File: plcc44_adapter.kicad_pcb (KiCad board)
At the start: 2 copper layers, 25.4 x 52.1 mm, 2 parts, among them U1 ATmega8515-16JU, U2 PIC16F74-IP

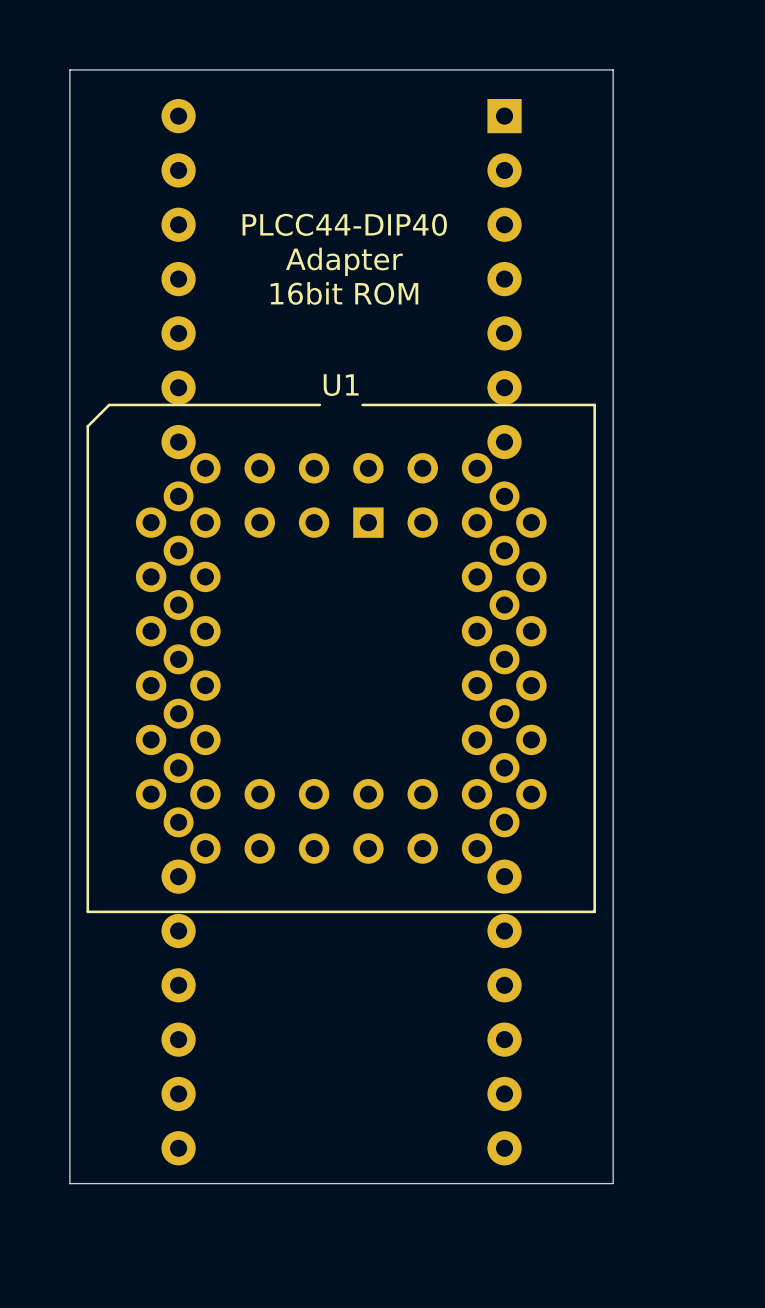
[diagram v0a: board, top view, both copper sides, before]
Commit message: Updated Symbols Updates Footprints for easier soldering
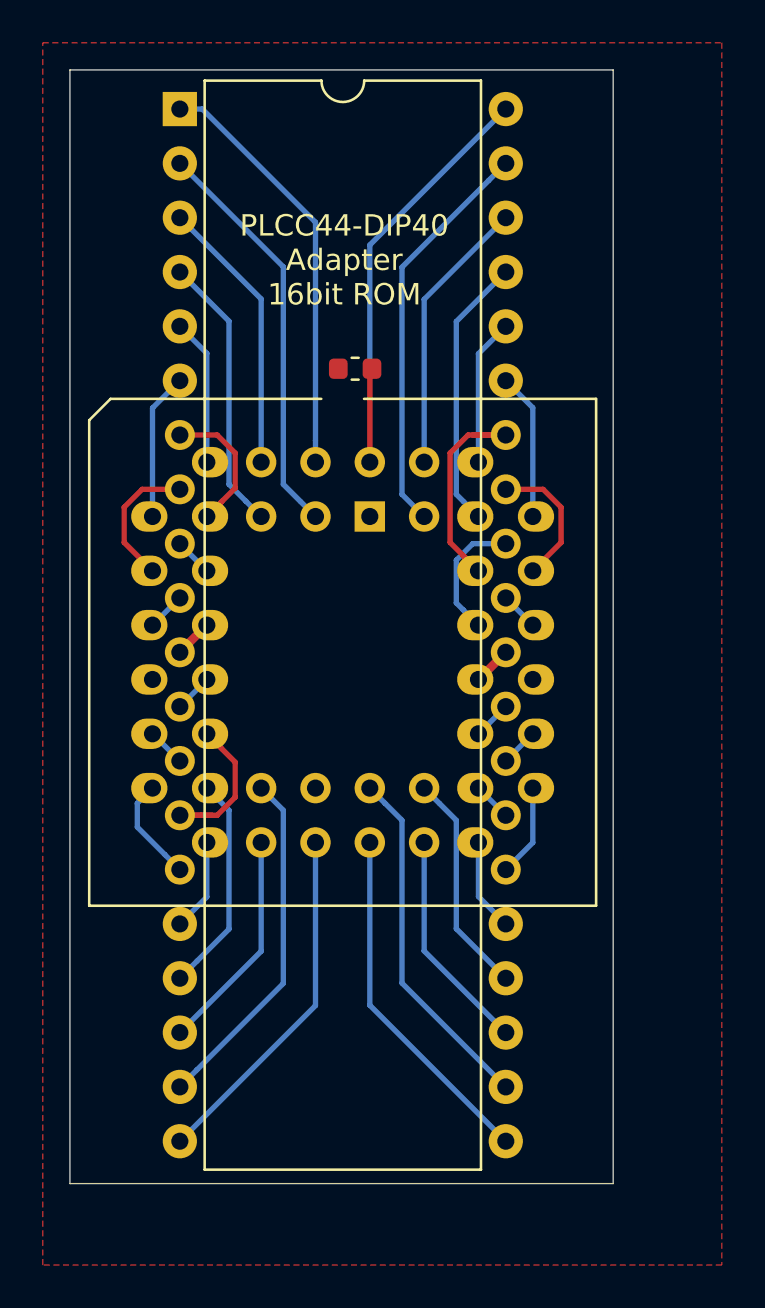
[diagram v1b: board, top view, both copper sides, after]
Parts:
- added C1: 100nF, Capacitor_SMD:C_0603_1608Metric, F.Cu at (173.4, 66.0)
- U1: value ATmega8515-16JU -> 16bit_rom; footprint Package_LCC:PLCC-44_THT-Socket -> dip40_mod:PLCC-44_THT-Socket_mod
- U2: value PIC16F74-IP -> 16bit_rom_dip40; footprint Package_DIP:DIP-40_W15.24mm -> dip40_mod:DIP-40_W15.24mm_mod; moved to F.Cu
- moved U2 15.2 mm to (165.2, 53.9), turned to 0 degrees
- moved U1 0.29 mm to (174.0, 72.9)
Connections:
- U1 pad 1: Net-(U1-Pad1) -> (no net)
- U1 pad 12: Net-(U1-Pad12) -> GND
- U1 pad 13: Net-(U1-Pad13) -> (no net)
- U1 pad 23: Net-(U1-Pad23) -> (no net)
- U1 pad 33: Net-(U1-Pad33) -> (no net)
- U1 pad 34: Net-(U1-Pad34) -> GND
- U1 pad 44: Net-(U1-Pad44) -> Net-(C1-Pad1)
- U2 pad 1: Net-(U2-Pad1) -> Net-(U1-Pad2)
- U2 pad 10: Net-(U2-Pad10) -> Net-(U1-Pad11)
- U2 pad 11: Net-(U2-Pad11) -> GND
- U2 pad 12: Net-(U2-Pad12) -> Net-(U1-Pad14)
- U2 pad 13: Net-(U2-Pad13) -> Net-(U1-Pad15)
- U2 pad 14: Net-(U2-Pad14) -> Net-(U1-Pad16)
- U2 pad 15: Net-(U2-Pad15) -> Net-(U1-Pad17)
- U2 pad 16: Net-(U2-Pad16) -> Net-(U1-Pad18)
- U2 pad 17: Net-(U2-Pad17) -> Net-(U1-Pad19)
- U2 pad 18: Net-(U2-Pad18) -> Net-(U1-Pad20)
- U2 pad 19: Net-(U2-Pad19) -> Net-(U1-Pad21)
- U2 pad 2: Net-(U2-Pad2) -> Net-(U1-Pad3)
- U2 pad 20: Net-(U2-Pad20) -> Net-(U1-Pad22)
- U2 pad 21: Net-(U2-Pad21) -> Net-(U1-Pad24)
- U2 pad 22: Net-(U2-Pad22) -> Net-(U1-Pad25)
- U2 pad 23: Net-(U2-Pad23) -> Net-(U1-Pad26)
- U2 pad 24: Net-(U2-Pad24) -> Net-(U1-Pad27)
- U2 pad 25: Net-(U2-Pad25) -> Net-(U1-Pad28)
- U2 pad 26: Net-(U2-Pad26) -> Net-(U1-Pad29)
- U2 pad 27: Net-(U2-Pad27) -> Net-(U1-Pad30)
- U2 pad 28: Net-(U2-Pad28) -> Net-(U1-Pad31)
- U2 pad 29: Net-(U2-Pad29) -> Net-(U1-Pad32)
- U2 pad 3: Net-(U2-Pad3) -> Net-(U1-Pad4)
- U2 pad 30: Net-(U2-Pad30) -> GND
- U2 pad 31: Net-(U2-Pad31) -> Net-(U1-Pad35)
- U2 pad 32: Net-(U2-Pad32) -> Net-(U1-Pad36)
- U2 pad 33: Net-(U2-Pad33) -> Net-(U1-Pad37)
- U2 pad 34: Net-(U2-Pad34) -> Net-(U1-Pad38)
- U2 pad 35: Net-(U2-Pad35) -> Net-(U1-Pad39)
- U2 pad 36: Net-(U2-Pad36) -> Net-(U1-Pad40)
- U2 pad 37: Net-(U2-Pad37) -> Net-(U1-Pad41)
- U2 pad 38: Net-(U2-Pad38) -> Net-(U1-Pad42)
- U2 pad 39: Net-(U2-Pad39) -> Net-(U1-Pad43)
- U2 pad 4: Net-(U2-Pad4) -> Net-(U1-Pad5)
- U2 pad 40: Net-(U2-Pad40) -> Net-(C1-Pad1)
- U2 pad 5: Net-(U2-Pad5) -> Net-(U1-Pad6)
- U2 pad 6: Net-(U2-Pad6) -> Net-(U1-Pad7)
- U2 pad 7: Net-(U2-Pad7) -> Net-(U1-Pad8)
- U2 pad 8: Net-(U2-Pad8) -> Net-(U1-Pad9)
- U2 pad 9: Net-(U2-Pad9) -> Net-(U1-Pad10)
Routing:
- net Net-(C1-Pad1): track 0.00 -> 23.7 mm
- net Net-(U1-Pad2): track 0.00 -> 19.8 mm
- net Net-(U1-Pad3): track 0.00 -> 19.1 mm
- net Net-(U1-Pad43): track 0.00 -> 18.9 mm
- net Net-(U1-Pad25): track 0.00 -> 16.6 mm
- net Net-(U1-Pad24): track 0.00 -> 16.6 mm
- net Net-(U1-Pad22): track 0.00 -> 16.6 mm
- net Net-(U1-Pad21): track 0.00 -> 16.4 mm
- net Net-(U1-Pad42): track 0.00 -> 13.0 mm
- net Net-(U1-Pad5): track 0.00 -> 13.0 mm
- net Net-(U1-Pad4): track 0.00 -> 13.0 mm
- net Net-(U1-Pad41): track 0.00 -> 12.8 mm
- net Net-(U1-Pad38): track 0.00 -> 11.6 mm
- net Net-(U1-Pad27): track 0.00 -> 10.5 mm
- net Net-(U1-Pad26): track 0.00 -> 10.5 mm
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- added copper zone on F.Cu, net GND
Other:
- net class GND added: clearance 0.2, trace_width 0.4, via_dia 0.8, via_drill 0.4

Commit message: Added Gerber Files Updated README Updated Layout
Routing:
- net Net-(C1-Pad1): track 23.7 -> 19.4 mm, vias 0 -> 1
- net Net-(U1-Pad17): track 4.93 -> 4.34 mm
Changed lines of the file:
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@@
     (thickness 1.6)
     (drawings 6)
-    (tracks 122)
+    (tracks 125)
     (zones 0)
     (modules 3)
@@
       (outputformat 1)
       (mirror false)
-      (drillshape 1)
+      (drillshape 0)
       (scaleselection 1)
-      (outputdirectory ""))
+      (outputdirectory "gerber"))
   )
   (net 0 "")
@@
   (gr_line (start 160.02 104.14) (end 185.42 104.14) (layer Edge.Cuts) (width 0.05))
   (gr_line (start 160.02 52.07) (end 160.02 104.14) (layer Edge.Cuts) (width 0.05))
+  (segment (start 170.2054 71.6534) (end 170.789601 72.237601) (width 0.25) (layer B.Cu) (net 1))
+  (segment (start 165.159001 56.439001) (end 170.2054 61.4854) (width 0.25) (layer B.Cu) (net 1))
   (segment (start 170.789601 72.237601) (end 171.5008 72.9488) (width 0.25) (layer B.Cu) (net 1))
-  (segment (start 169.997001 71.445001) (end 170.789601 72.237601) (width 0.25) (layer B.Cu) (net 1))
-  (segment (start 169.997001 61.277001) (end 169.997001 71.445001) (width 0.25) (layer B.Cu) (net 1))
-  (segment (start 165.159001 56.439001) (end 169.997001 61.277001) (width 0.25) (layer B.Cu) (net 1))
-  (segment (start 167.457001 71.445001) (end 168.249601 72.237601) (width 0.25) (layer B.Cu) (net 2))
-  (segment (start 167.457001 63.817001) (end 167.457001 71.445001) (width 0.25) (layer B.Cu) (net 2))
+  (segment (start 170.2054 61.4854) (end 170.2054 71.6534) (width 0.25) (layer B.Cu) (net 1))
+  (segment (start 167.7924 71.7804) (end 168.249601 72.237601) (width 0.25) (layer B.Cu) (net 2))
+  (segment (start 165.159001 61.519001) (end 167.7924 64.1524) (width 0.25) (layer B.Cu) (net 2))
   (segment (start 168.249601 72.237601) (end 168.9608 72.9488) (width 0.25) (layer B.Cu) (net 2))
-  (segment (start 165.159001 61.519001) (end 167.457001 63.817001) (width 0.25) (layer B.Cu) (net 2))
+  (segment (start 167.7924 64.1524) (end 167.7924 71.7804) (width 0.25) (layer B.Cu) (net 2))
   (segment (start 179.599002 57.239) (end 180.399001 56.439001) (width 0.25) (layer B.Cu) (net 3))
-  (segment (start 175.544599 61.293403) (end 179.599002 57.239) (width 0.25) (layer B.Cu) (net 3))
-  (segment (start 175.544599 71.912599) (end 175.544599 61.293403) (width 0.25) (layer B.Cu) (net 3))
-  (segment (start 176.5808 72.9488) (end 175.544599 71.912599) (width 0.25) (layer B.Cu) (net 3))
+  (segment (start 175.3108 61.527202) (end 179.599002 57.239) (width 0.25) (layer B.Cu) (net 3))
+  (segment (start 176.5808 72.9488) (end 175.3108 71.6788) (width 0.25) (layer B.Cu) (net 3))
+  (segment (start 175.3108 71.6788) (end 175.3108 61.527202) (width 0.25) (layer B.Cu) (net 3))
   (segment (start 178.409601 72.237601) (end 179.1208 72.9488) (width 0.25) (layer B.Cu) (net 4))
-  (segment (start 178.084599 63.833403) (end 178.084599 71.912599) (width 0.25) (layer B.Cu) (net 4))
-  (segment (start 178.084599 71.912599) (end 178.409601 72.237601) (width 0.25) (layer B.Cu) (net 4))
-  (segment (start 180.399001 61.519001) (end 178.084599 63.833403) (width 0.25) (layer B.Cu) (net 4))
+  (segment (start 180.399001 61.519001) (end 177.673 64.245002) (width 0.25) (layer B.Cu) (net 4))
+  (segment (start 177.673 71.501) (end 178.409601 72.237601) (width 0.25) (layer B.Cu) (net 4))
+  (segment (start 177.673 64.245002) (end 177.673 71.501) (width 0.25) (layer B.Cu) (net 4))
   (segment (start 171.5008 59.1908) (end 171.5008 69.403012) (width 0.25) (layer B.Cu) (net 5))
   (segment (start 166.209001 53.899001) (end 171.5008 59.1908) (width 0.25) (layer B.Cu) (net 5))
@@
   (segment (start 166.4208 70.4088) (end 166.4208 65.3208) (width 0.25) (layer B.Cu) (net 7))
   (segment (start 174.0408 60.257202) (end 180.399001 53.899001) (width 0.25) (layer B.Cu) (net 39))
-  (segment (start 174.0408 70.4088) (end 174.0408 60.257202) (width 0.25) (layer B.Cu) (net 39))
   (segment (start 176.5808 62.797202) (end 176.5808 70.4088) (width 0.25) (layer B.Cu) (net 8))
   (segment (start 180.399001 58.979001) (end 176.5808 62.797202) (width 0.25) (layer B.Cu) (net 8))
@@
   (segment (start 163.8888 83.1088) (end 165.159001 84.379001) (width 0.25) (layer B.Cu) (net 16))
   (segment (start 163.8808 83.1088) (end 163.8888 83.1088) (width 0.25) (layer B.Cu) (net 16))
+  (segment (start 163.8808 85.6488) (end 163.8808 88.1808) (width 0.25) (layer B.Cu) (net 17))
   (segment (start 164.459002 88.759002) (end 165.159001 89.459001) (width 0.25) (layer B.Cu) (net 17))
-  (segment (start 163.169601 86.359999) (end 163.169601 87.469601) (width 0.25) (layer B.Cu) (net 17))
-  (segment (start 163.169601 87.469601) (end 164.459002 88.759002) (width 0.25) (layer B.Cu) (net 17))
-  (segment (start 163.8808 85.6488) (end 163.169601 86.359999) (width 0.25) (layer B.Cu) (net 17))
+  (segment (start 163.8808 88.1808) (end 164.459002 88.759002) (width 0.25) (layer B.Cu) (net 17))
+  (segment (start 167.8178 91.880202) (end 165.959 93.739002) (width 0.25) (layer B.Cu) (net 18))
   (segment (start 165.959 93.739002) (end 165.159001 94.539001) (width 0.25) (layer B.Cu) (net 18))
-  (segment (start 167.457001 92.241001) (end 165.959 93.739002) (width 0.25) (layer B.Cu) (net 18))
-  (segment (start 167.457001 86.685001) (end 167.457001 92.241001) (width 0.25) (layer B.Cu) (net 18))
-  (segment (start 166.4208 85.6488) (end 167.457001 86.685001) (width 0.25) (layer B.Cu) (net 18))
+  (segment (start 166.4208 85.6488) (end 167.8178 87.0458) (width 0.25) (layer B.Cu) (net 18))
+  (segment (start 167.8178 87.0458) (end 167.8178 91.880202) (width 0.25) (layer B.Cu) (net 18))
   (segment (start 165.959 98.819002) (end 165.159001 99.619001) (width 0.25) (layer B.Cu) (net 19))
-  (segment (start 169.997001 94.781001) (end 165.959 98.819002) (width 0.25) (layer B.Cu) (net 19))
-  (segment (start 169.997001 86.685001) (end 169.997001 94.781001) (width 0.25) (layer B.Cu) (net 19))
-  (segment (start 168.9608 85.6488) (end 169.997001 86.685001) (width 0.25) (layer B.Cu) (net 19))
-  (segment (start 175.544599 87.152599) (end 174.751999 86.359999) (width 0.25) (layer B.Cu) (net 20))
+  (segment (start 170.2054 94.572602) (end 165.959 98.819002) (width 0.25) (layer B.Cu) (net 19))
+  (segment (start 168.9608 85.6488) (end 170.2054 86.8934) (width 0.25) (layer B.Cu) (net 19))
+  (segment (start 170.2054 86.8934) (end 170.2054 94.572602) (width 0.25) (layer B.Cu) (net 19))
   (segment (start 174.751999 86.359999) (end 174.0408 85.6488) (width 0.25) (layer B.Cu) (net 20))
-  (segment (start 175.544599 94.764599) (end 175.544599 87.152599) (width 0.25) (layer B.Cu) (net 20))
-  (segment (start 180.399001 99.619001) (end 175.544599 94.764599) (width 0.25) (layer B.Cu) (net 20))
+  (segment (start 180.399001 99.619001) (end 175.3362 94.5562) (width 0.25) (layer B.Cu) (net 20))
+  (segment (start 175.3362 86.9442) (end 174.751999 86.359999) (width 0.25) (layer B.Cu) (net 20))
+  (segment (start 175.3362 94.5562) (end 175.3362 86.9442) (width 0.25) (layer B.Cu) (net 20))
   (segment (start 177.291999 86.359999) (end 176.5808 85.6488) (width 0.25) (layer B.Cu) (net 21))
-  (segment (start 178.084599 87.152599) (end 177.291999 86.359999) (width 0.25) (layer B.Cu) (net 21))
-  (segment (start 178.084599 92.224599) (end 178.084599 87.152599) (width 0.25) (layer B.Cu) (net 21))
-  (segment (start 180.399001 94.539001) (end 178.084599 92.224599) (width 0.25) (layer B.Cu) (net 21))
+  (segment (start 180.399001 94.539001) (end 177.673 91.813) (width 0.25) (layer B.Cu) (net 21))
+  (segment (start 177.673 86.741) (end 177.291999 86.359999) (width 0.25) (layer B.Cu) (net 21))
+  (segment (start 177.673 91.813) (end 177.673 86.741) (width 0.25) (layer B.Cu) (net 21))
   (segment (start 181.6608 88.197202) (end 181.6608 85.6488) (width 0.25) (layer B.Cu) (net 22))
   (segment (start 180.399001 89.459001) (end 181.6608 88.197202) (width 0.25) (layer B.Cu) (net 22))
@@
   (segment (start 179.129202 83.1088) (end 180.399001 81.839001) (width 0.25) (layer B.Cu) (net 30))
   (segment (start 179.1208 83.1088) (end 179.129202 83.1088) (width 0.25) (layer B.Cu) (net 30))
-  (segment (start 178.409601 77.317601) (end 179.1208 78.0288) (width 0.25) (layer B.Cu) (net 31))
-  (segment (start 178.084599 74.991423) (end 178.084599 76.992599) (width 0.25) (layer B.Cu) (net 31))
-  (segment (start 178.084599 76.992599) (end 178.409601 77.317601) (width 0.25) (layer B.Cu) (net 31))
-  (segment (start 178.857021 74.219001) (end 178.084599 74.991423) (width 0.25) (layer B.Cu) (net 31))
-  (segment (start 180.399001 74.219001) (end 178.857021 74.219001) (width 0.25) (layer B.Cu) (net 31))
+  (segment (start 179.409052 74.219001) (end 180.399001 74.219001) (width 0.25) (layer B.Cu) (net 31))
+  (segment (start 178.636377 74.219001) (end 179.409052 74.219001) (width 0.25) (layer B.Cu) (net 31))
+  (segment (start 177.79579 75.059588) (end 178.636377 74.219001) (width 0.25) (layer B.Cu) (net 31))
+  (segment (start 177.79579 76.70379) (end 177.79579 75.059588) (width 0.25) (layer B.Cu) (net 31))
+  (segment (start 179.1208 78.0288) (end 177.79579 76.70379) (width 0.25) (layer B.Cu) (net 31))
   (segment (start 178.409601 74.777601) (end 179.1208 75.4888) (width 0.25) (layer F.Cu) (net 32))
   (segment (start 180.399001 69.139001) (end 178.857021 69.139001) (width 0.25) (layer F.Cu) (net 32))
@@
   (segment (start 174.0408 66.1417) (end 174.1425 66.04) (width 0.25) (layer F.Cu) (net 39))
   (segment (start 174.0408 70.4088) (end 174.0408 66.1417) (width 0.25) (layer F.Cu) (net 39))
+  (via (at 173.99 64.77) (size 0.8) (drill 0.4) (layers F.Cu B.Cu) (net 39))
+  (segment (start 174.0408 60.257202) (end 174.0408 64.7192) (width 0.25) (layer B.Cu) (net 39))
+  (segment (start 174.0408 64.7192) (end 173.99 64.77) (width 0.25) (layer B.Cu) (net 39))
+  (segment (start 173.99 65.8875) (end 174.1425 66.04) (width 0.25) (layer F.Cu) (net 39))
+  (segment (start 173.99 64.77) (end 173.99 65.8875) (width 0.25) (layer F.Cu) (net 39))
   (zone (net 38) (net_name GND) (layer F.Cu) (hatch edge 0.508)
     (connect_pads (clearance 0.254))
